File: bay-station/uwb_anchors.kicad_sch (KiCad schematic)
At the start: 16 parts, among them U4 DWM3000, U5 DWM3000, U6 DWM3000, U7 DWM3000

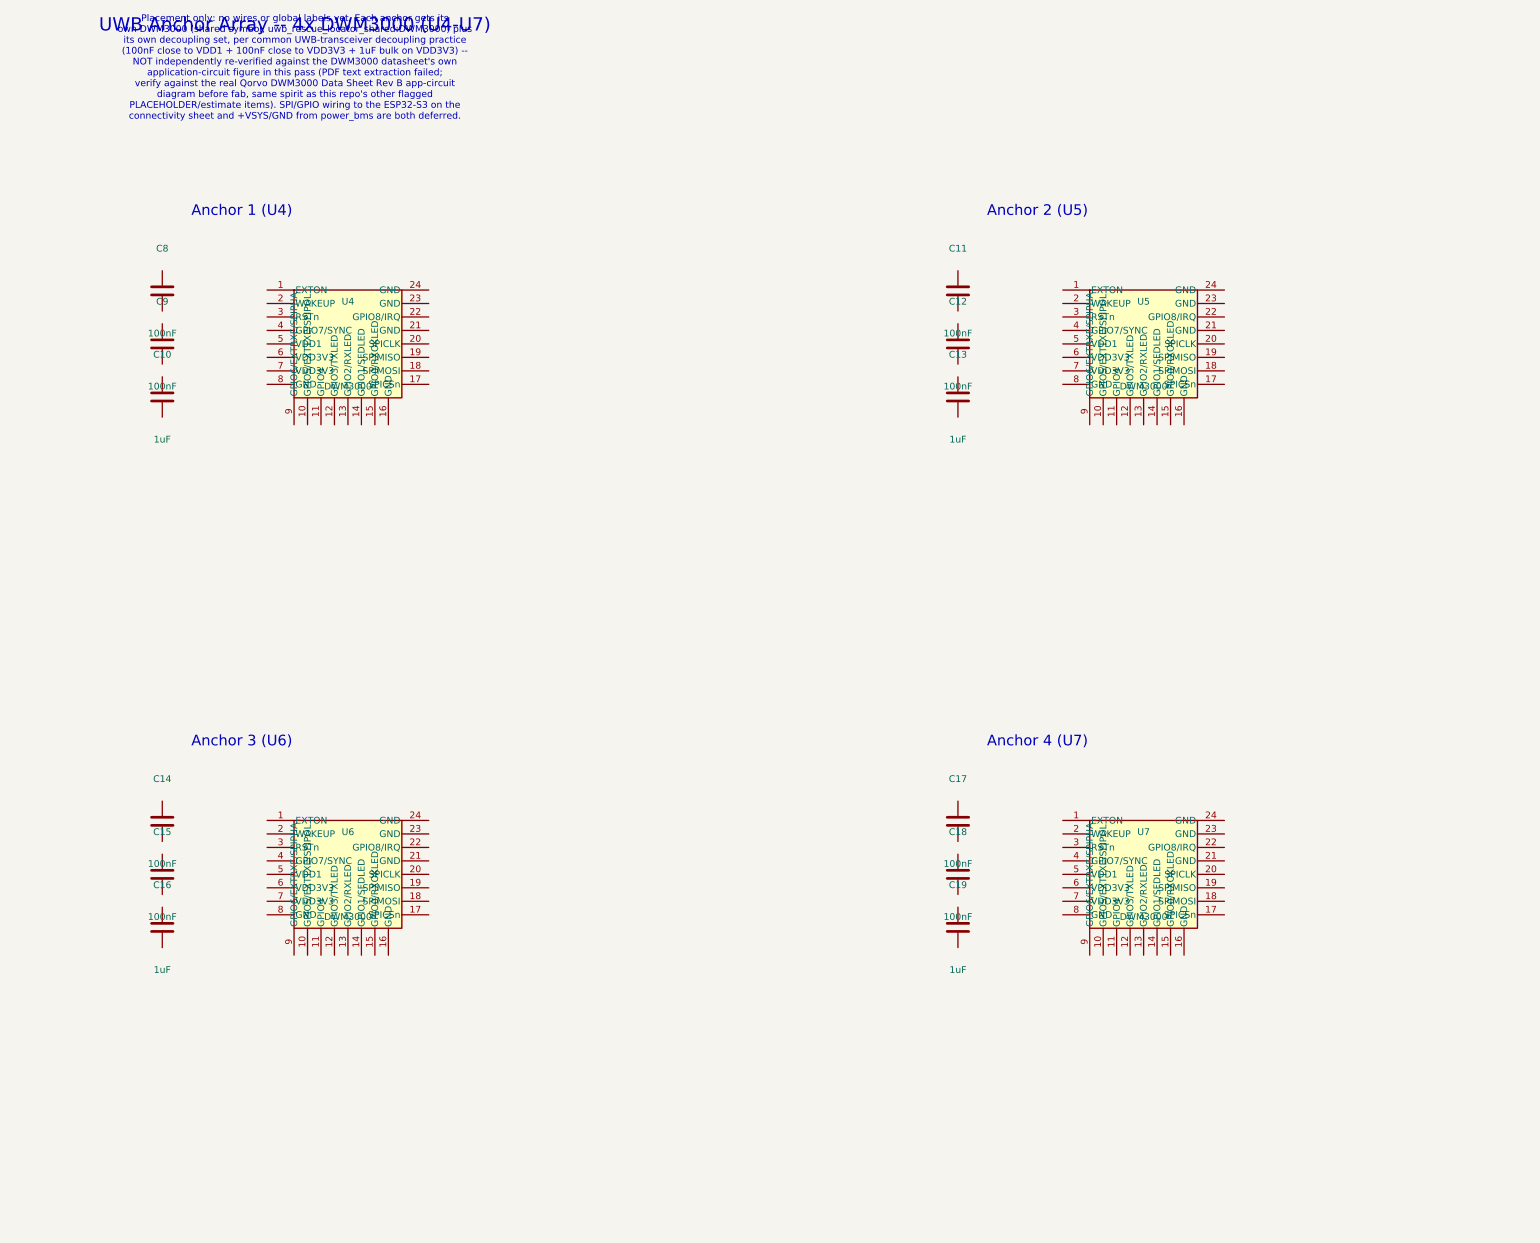
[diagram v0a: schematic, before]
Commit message: Add regulation/antenna/programming-debug sheets; fix confirmed voltage-safety gap
Real datasheet check found a genuine hardware bug in progress, not just a
missing part: NINA-B111 abs-max VCC is 3.9V, DWM3000 abs-max VDD3V3 is
4.0V, but a fully-charged LiPo hits 4.2V -- both boards were about to feed
these ICs straight off the unregulated battery/system rail. Fixed via a
new dedicated regulation sheet per board (placement-only, not wired yet,
same as everything else at this stage):

- wristband/regulation.kicad_sch: MCP1700T-3302E/TT LDO (3.3V, low-Iq),
  current budget verified (NINA-B111 ~12mA + DWM3000 ~55mA vs 250mA
  rating, ~3.7x headroom)
- bay-station/regulation.kicad_sch: TPS62A02PDDCR buck converter (2A,
  single-cell-Li-Ion input range -- the very common TPS563201 was
  considered and rejected, its 4.5V input minimum is incompatible with a
  battery-only rail), current budget verified (ESP32-S3 ~355mA peak +
  4x DWM3000 ~55mA each vs 2A rating, ~3.5x headroom)

Also added, all confirmed against real datasheets:
- wristband/antenna.kicad_sch: ProAnt InSide-2400 BLE antenna (NINA-B111
  needs an external one per u-blox's approved-antenna list; DWM3000 has
  its own onboard antenna already, confirmed, no antenna sheet needed on
  the bay station)
- GPIO5/6 SPI-mode strapping pull-downs on every DWM3000 instance (both
  boards) -- required per Qorvo's own power-up timing diagrams
- wristband/programming_debug.kicad_sch: SWD header for NINA-B111
- bay-station/programming_debug.kicad_sch: ESP32-S3 boot-strap resistors,
  EN RC delay, BOOT/RESET buttons, native-USB flashing interface

One real inconsistency surfaced and flagged (not fixed) in
docs/decisions.md: the bay station's existing power-input USB-C has no
data pins, so a second, data-capable USB-C had to be added for ESP32-S3
flashing rather than consolidating into one connector -- needs a decision.

docs/decisions.md and README.md updated: new items marked resolved with
full reasoning, new open items ad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
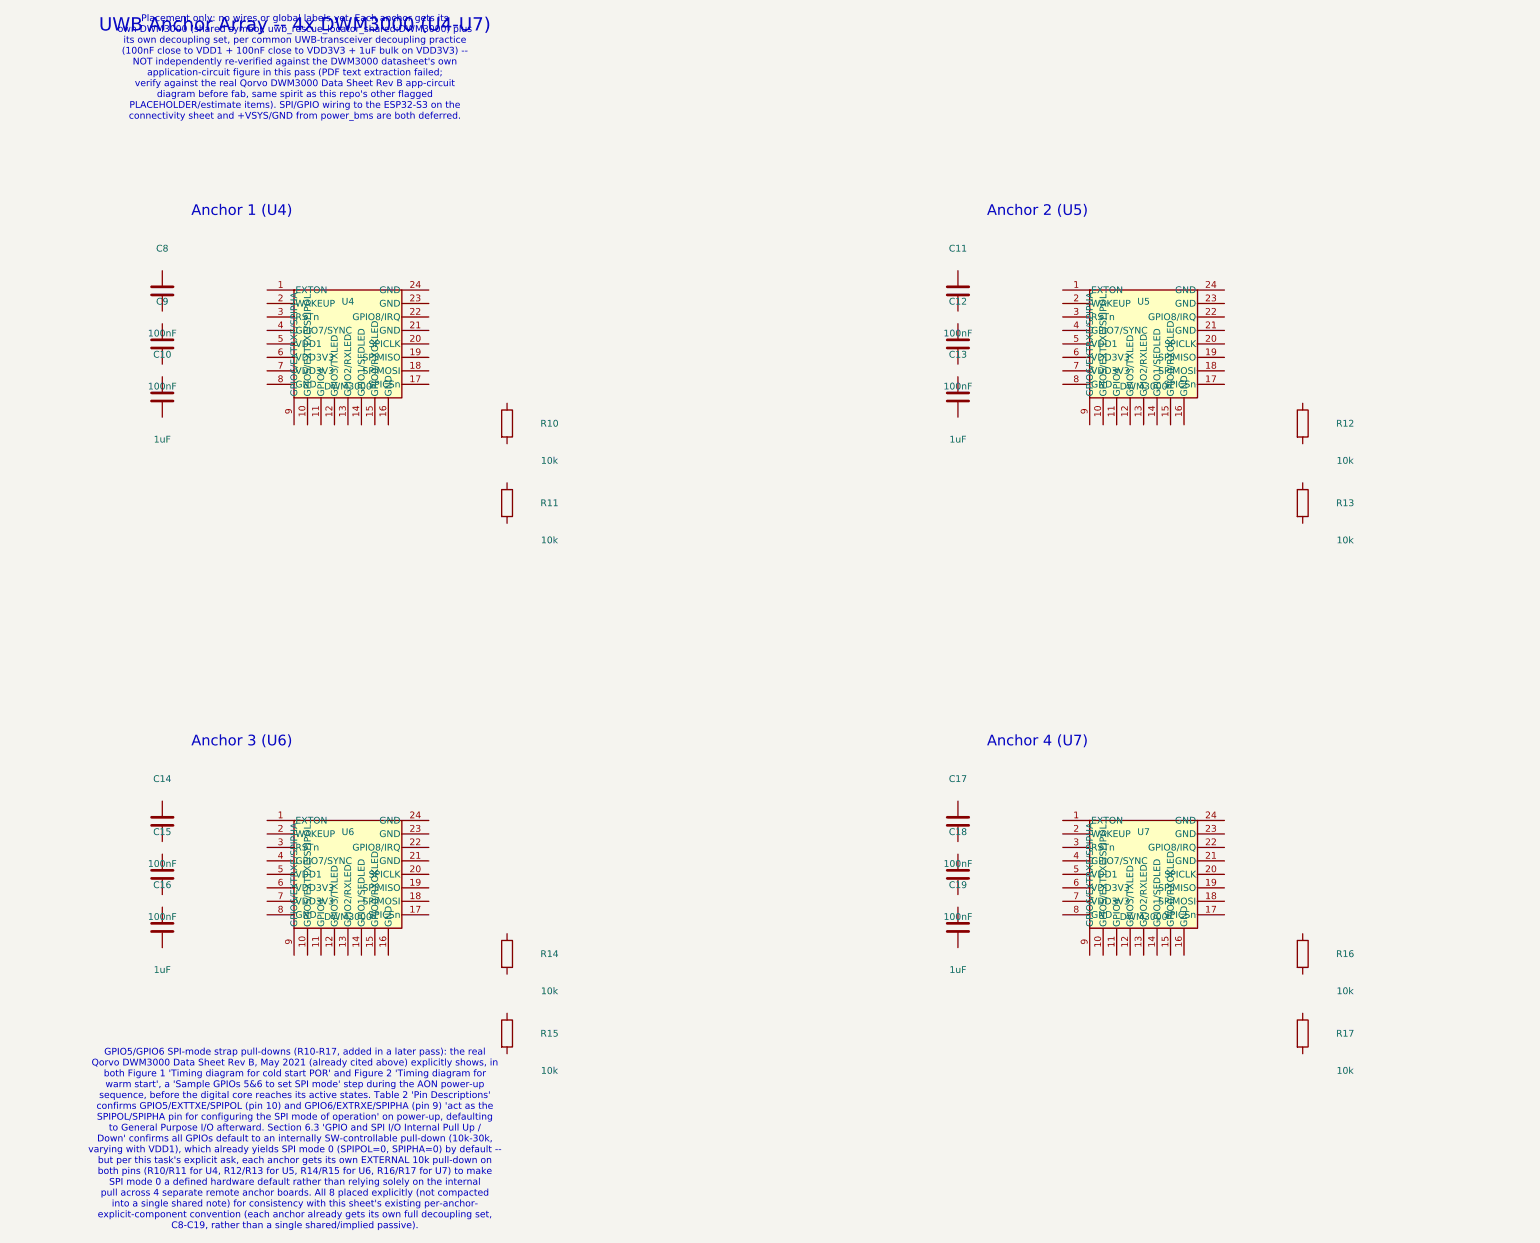
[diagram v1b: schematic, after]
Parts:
- added R10, R11, R12, R13, R14, R15, R16, R17: 10k, Resistor_SMD:R_0603_1608Metric, symbol Device:R
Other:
- note added: "GPIO5/GPIO6 SPI-mode strap pull-downs (R10-R17, added in a later pass): the real Qorvo DWM3000 Data Sheet Rev B, May 2021 (already cited above) explicitly shows, in both Figure 1 'Timing diagram for cold start POR' and Figure 2 'Timing diagram for warm start', a 'Sample GPIOs 5&6 to set SPI mode' step during the AON power-up sequence, before the digital core reaches its active states. Table 2 'Pi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"

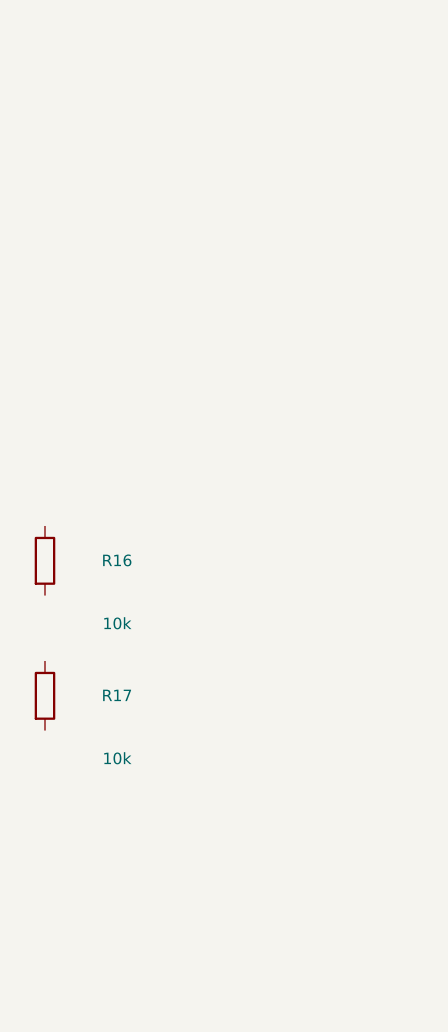
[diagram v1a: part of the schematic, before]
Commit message: Compile passives reference from each chip's real datasheet reference design
New docs/passives-reference.md: per-chip table of every passive called for
by that chip's own real reference/typical-application circuit (not
guessed), cross-referencing what's already placed vs. what the datasheet
actually shows.

Found and fixed one real gap while doing this: Qorvo's own DWM3000
'Example Application Circuit' (Figure 11) shows a 100k pulldown on
IRQ/GPIO8 'to prevent spurious interrupts' -- missing from the design
entirely until now. Added as R9 (wristband/radio_mcu.kicad_sch) and
R25-R28, one per anchor (bay-station/uwb_anchors.kicad_sch).

Also documented two nuances found by reading the same figure closely,
neither of which needed a design change:
- DWM3000's placed decoupling caps go beyond what Qorvo's own minimal
  application circuit shows (the module needs 'only power' per the
  datasheet's own text) -- kept as reasonable conservative practice.
- The GPIO5/6 external strap pull-downs already placed are redundant with
  the chip's own internal default pull-downs (10-30k, varies with VDD1)
  confirmed via the datasheet's GPIO pull-up/down section -- kept
  deliberately for tighter, more deterministic timing margin.

Confirmed via NINA-B1 series datasheet Section 2.1.1: the module has
fully integrated on-board LDO+buck regulation, so needs no external
regulation for its own internal rails (doesn't contradict the external
LDO already added -- that protects the VCC input pin itself from
exceeding its absolute max, a separate concern from internal regulation).

README.md and docs/decisions.md updated to reference the new document and
mark the decoupling-verification 'not done yet' item resolved.
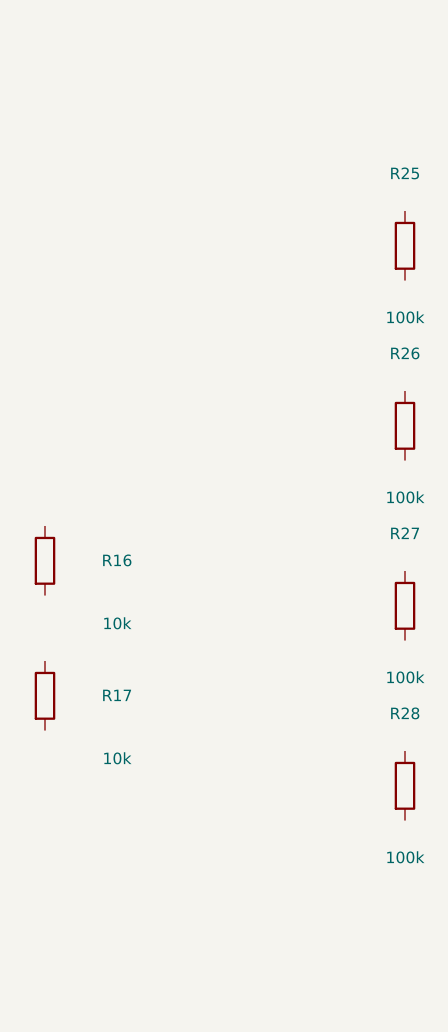
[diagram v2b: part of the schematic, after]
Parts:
- added R25, R26, R27, R28: 100k, Resistor_SMD:R_0603_1608Metric, symbol Device:R
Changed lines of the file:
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@@
+		)
+	)
+	(symbol
+		(lib_id "Device:R")
+		(at 290.0 170.0 0)
+		(unit 1)
+		(exclude_from_sim no)
+		(in_bom yes)
+		(on_board yes)
+		(dnp no)
+		(property "Reference" "R25"
+			(at 290.0 162.0 0)
+			(effects
+				(font
+					(size 1.27 1.27)
+				)
+			)
+		)
+		(property "Value" "100k"
+			(at 290.0 178.0 0)
+			(effects
+				(font
+					(size 1.27 1.27)
+				)
+			)
+		)
+		(property "Footprint" "Resistor_SMD:R_0603_1608Metric"
+			(at 290.0 170.0 0)
+			(effects
+				(font
+					(size 1.27 1.27)
+				)
+				(hide yes)
+			)
+		)
+		(property "Datasheet" ""
+			(at 290.0 170.0 0)
+			(effects
+				(font
+					(size 1.27 1.27)
+				)
+				(hide yes)
+			)
+		)
+		(pin "1"
+		)
+		(pin "2"
+		)
+		(instances
+			(project "bay-station"
+				(path "/543ba435-6cf4-448c-821e-3c5778b02e9c/7a56b57e-fbec-43eb-be10-7a1a5f682193"
+					(reference "R25")
+					(unit 1)
+				)
+			)
+		)
+	)
+	(symbol
+		(lib_id "Device:R")
+		(at 290.0 190.0 0)
+		(unit 1)
+		(exclude_from_sim no)
+		(in_bom yes)
+		(on_board yes)
+		(dnp no)
+		(property "Reference" "R26"
+			(at 290.0 182.0 0)
+			(effects
+				(font
+					(size 1.27 1.27)
+				)
+			)
+		)
+		(property "Value" "100k"
+			(at 290.0 198.0 0)
+			(effects
+				(font
+					(size 1.27 1.27)
+				)
+			)
+		)
+		(property "Footprint" "Resistor_SMD:R_0603_1608Metric"
+			(at 290.0 190.0 0)
+			(effects
+				(font
+					(size 1.27 1.27)
+				)
+				(hide yes)
+			)
+		)
+		(property "Datasheet" ""
+			(at 290.0 190.0 0)
+			(effects
+				(font
+					(size 1.27 1.27)
+				)
+				(hide yes)
+			)
+		)
+		(pin "1"
+		)
+		(pin "2"
+		)
+		(instances
+			(project "bay-station"
+				(path "/543ba435-6cf4-448c-821e-3c5778b02e9c/7a56b57e-fbec-43eb-be10-7a1a5f682193"
+					(reference "R26")
+					(unit 1)
+				)
+			)
+		)
+	)
+	(symbol
+		(lib_id "Device:R")
+		(at 290.0 210.0 0)
+		(unit 1)
+		(exclude_from_sim no)
+		(in_bom yes)
+		(on_board yes)
+		(dnp no)
+		(property "Reference" "R27"
+			(at 290.0 202.0 0)
+			(effects
+				(font
+					(size 1.27 1.27)
+				)
+			)
+		)
+		(property "Value" "100k"
+			(at 290.0 218.0 0)
+			(effects
+				(font
+					(size 1.27 1.27)
+				)
+			)
+		)
+		(property "Footprint" "Resistor_SMD:R_0603_1608Metric"
+			(at 290.0 210.0 0)
+			(effects
+				(font
+					(size 1.27 1.27)
+				)
+				(hide yes)
+			)
+		)
+		(property "Datasheet" ""
+			(at 290.0 210.0 0)
+			(effects
+				(font
+					(size 1.27 1.27)
+				)
+				(hide yes)
+			)
+		)
+		(pin "1"
+		)
+		(pin "2"
+		)
+		(instances
+			(project "bay-station"
+				(path "/543ba435-6cf4-448c-821e-3c5778b02e9c/7a56b57e-fbec-43eb-be10-7a1a5f682193"
+					(reference "R27")
+					(unit 1)
+				)
+			)
+		)
+	)
+	(symbol
+		(lib_id "Device:R")
+		(at 290.0 230.0 0)
+		(unit 1)
+		(exclude_from_sim no)
+		(in_bom yes)
+		(on_board yes)
+		(dnp no)
+		(property "Reference" "R28"
+			(at 290.0 222.0 0)
+			(effects
+				(font
+					(size 1.27 1.27)
+				)
+			)
+		)
+		(property "Value" "100k"
+			(at 290.0 238.0 0)
+			(effects
+				(font
+					(size 1.27 1.27)
+				)
+			)
+		)
+		(property "Footprint" "Resistor_SMD:R_0603_1608Metric"
+			(at 290.0 230.0 0)
+			(effects
+				(font
+					(size 1.27 1.27)
+				)
+				(hide yes)
+			)
+		)
+		(property "Datasheet" ""
+			(at 290.0 230.0 0)
+			(effects
+				(font
+					(size 1.27 1.27)
+				)
+				(hide yes)
+			)
+		)
+		(pin "1"
+		)
+		(pin "2"
+		)
+		(instances
+			(project "bay-station"
+				(path "/543ba435-6cf4-448c-821e-3c5778b02e9c/7a56b57e-fbec-43eb-be10-7a1a5f682193"
+					(reference "R28")
+					(unit 1)
+				)
+			)
 		)
 	)
